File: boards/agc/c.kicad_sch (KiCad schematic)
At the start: 3 parts, among them Q5 MMBT2222

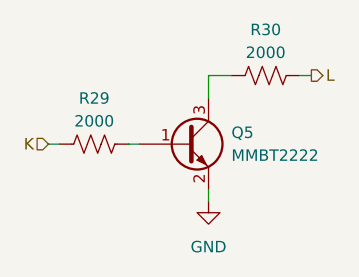
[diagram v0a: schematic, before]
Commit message: Add PSA switching modules and rework fine ref
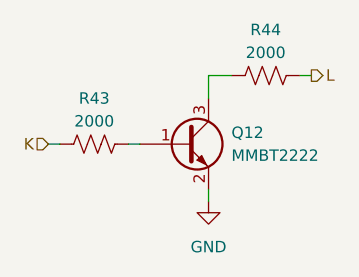
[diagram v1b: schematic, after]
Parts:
- renumbered Q5 to Q12, R29 to R43, R30 to R44
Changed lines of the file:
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@@
 (kicad_sch
-	(version 20231120)
+	(version 20250114)
 	(generator "eeschema")
-	(generator_version "8.0")
+	(generator_version "9.0")
 	(paper "A4")
 	(wire
@@
 		(shape output)
 		(at 111.76 87.63 0)
-		(fields_autoplaced yes)
 		(effects
 			(font
@@
 		(shape input)
 		(at 82.55 95.25 180)
-		(fields_autoplaced yes)
 		(effects
 			(font
@@
 		(on_board yes)
 		(dnp no)
-		(property "Reference" "R29"
+		(property "Reference" "R43"
 			(at 87.63 90.17 90)
 			(effects
@@
 		(dnp no)
 		(fields_autoplaced yes)
-		(property "Reference" "Q5"
+		(property "Reference" "Q12"
 			(at 102.87 93.9799 0)
 			(effects
@@
 		(dnp no)
 		(fields_autoplaced yes)
-		(property "Reference" "#PWR057"
+		(property "Reference" "#PWR041"
 			(at 100.33 107.95 0)
 			(effects
@@
 		(on_board yes)
 		(dnp no)
-		(property "Reference" "R30"
+		(property "Reference" "R44"
 			(at 106.68 82.55 90)
 			(effects
